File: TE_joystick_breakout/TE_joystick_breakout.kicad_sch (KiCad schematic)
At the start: 12 parts, among them J1 2434804-1, J2 Conn_01x04, J3 Conn_01x04, SW1 SW_Push

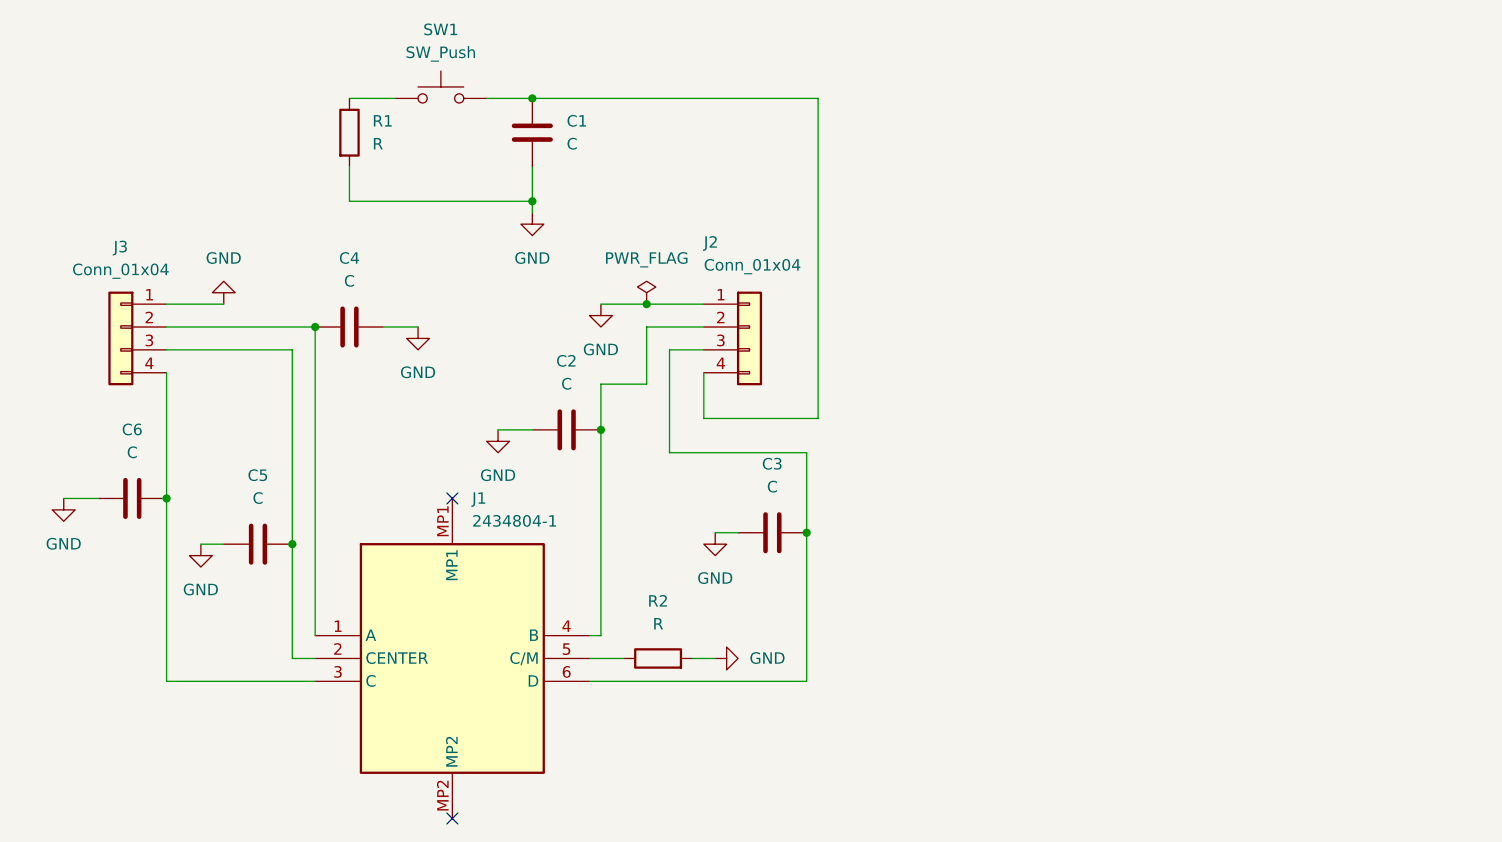
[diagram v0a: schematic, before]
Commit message: Redesign joystick breakout
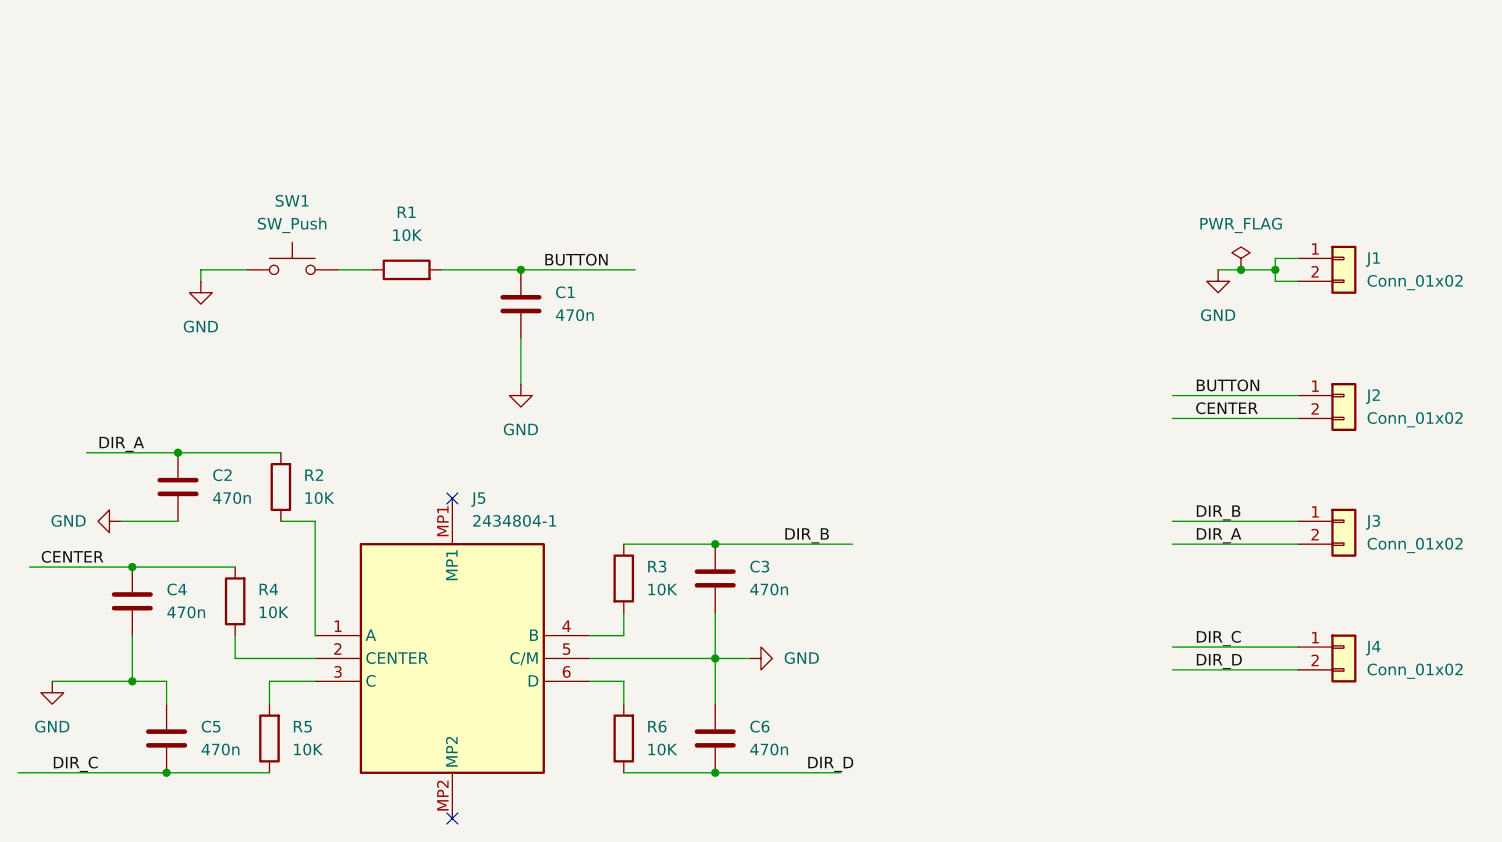
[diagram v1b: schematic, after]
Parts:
- removed C6: C, Capacitor_SMD:C_0402_1005Metric, symbol Device:C
- removed J2, J3: Conn_01x04, Connector_PinHeader_2.54mm:PinHeader_1x04_P2.54mm_Vertical, symbol Connector_Generic:Conn_01x04
- added C2: 470n, Capacitor_SMD:C_0402_1005Metric, symbol Device:C
- added J1, J2, J3, J4: Conn_01x02, Connector_PinHeader_2.54mm:PinHeader_1x02_P2.54mm_Vertical, symbol Connector_Generic:Conn_01x02
- added R3, R4, R5, R6: 10K, Resistor_SMD:R_0402_1005Metric, symbol Device:R
- C1, C4, C5: value C -> 470n
- C3: renamed from C2; value C -> 470n
- C6: renamed from C3; value C -> 470n
- R1, R2: value R -> 10K
- renumbered J1 to J5
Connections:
- net GND: now also C4.1, C5.2, C6.2, J5.5 (C/M), SW1.1, C2.1, J1.1 (Pin_1), J1.2 (Pin_2); no longer C4.2, C5.1, C6.1, R1.2, R2.2
- net at J5.2 (CENTER): now also R4.1; no longer C5.2
- net at J5.3 (C): now also R5.2
- net at J5.4 (B): now also R3.2; no longer C3.2
- net at J5.6 (D): now also R6.2; no longer C6.2
- net at SW1.2: now also R1.1; no longer C1.1
- net at R2.1: now also J5.1 (A); no longer J5.5 (C/M)
- new net BUTTON: C1.1, J2.1 (Pin_1), R1.2
- new net CENTER: C4.2, J2.2 (Pin_2), R4.2
- new net DIR_A: C2.2, J3.2 (Pin_2), R2.2
- new net DIR_B: C3.2, J3.1 (Pin_1), R3.1
- new net DIR_C: C5.1, J4.1 (Pin_1), R5.1
- new net DIR_D: C6.1, J4.2 (Pin_2), R6.1
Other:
- moved on the sheet: C1, C3, C6, R1, SW1
